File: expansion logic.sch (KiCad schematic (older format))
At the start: 30 parts, among them U302 74LS32, U800 BUSTER5721, U801 MSM6242, U802 74LS138, U803 74LS08, U804 74LS148, Y800 32768Hz

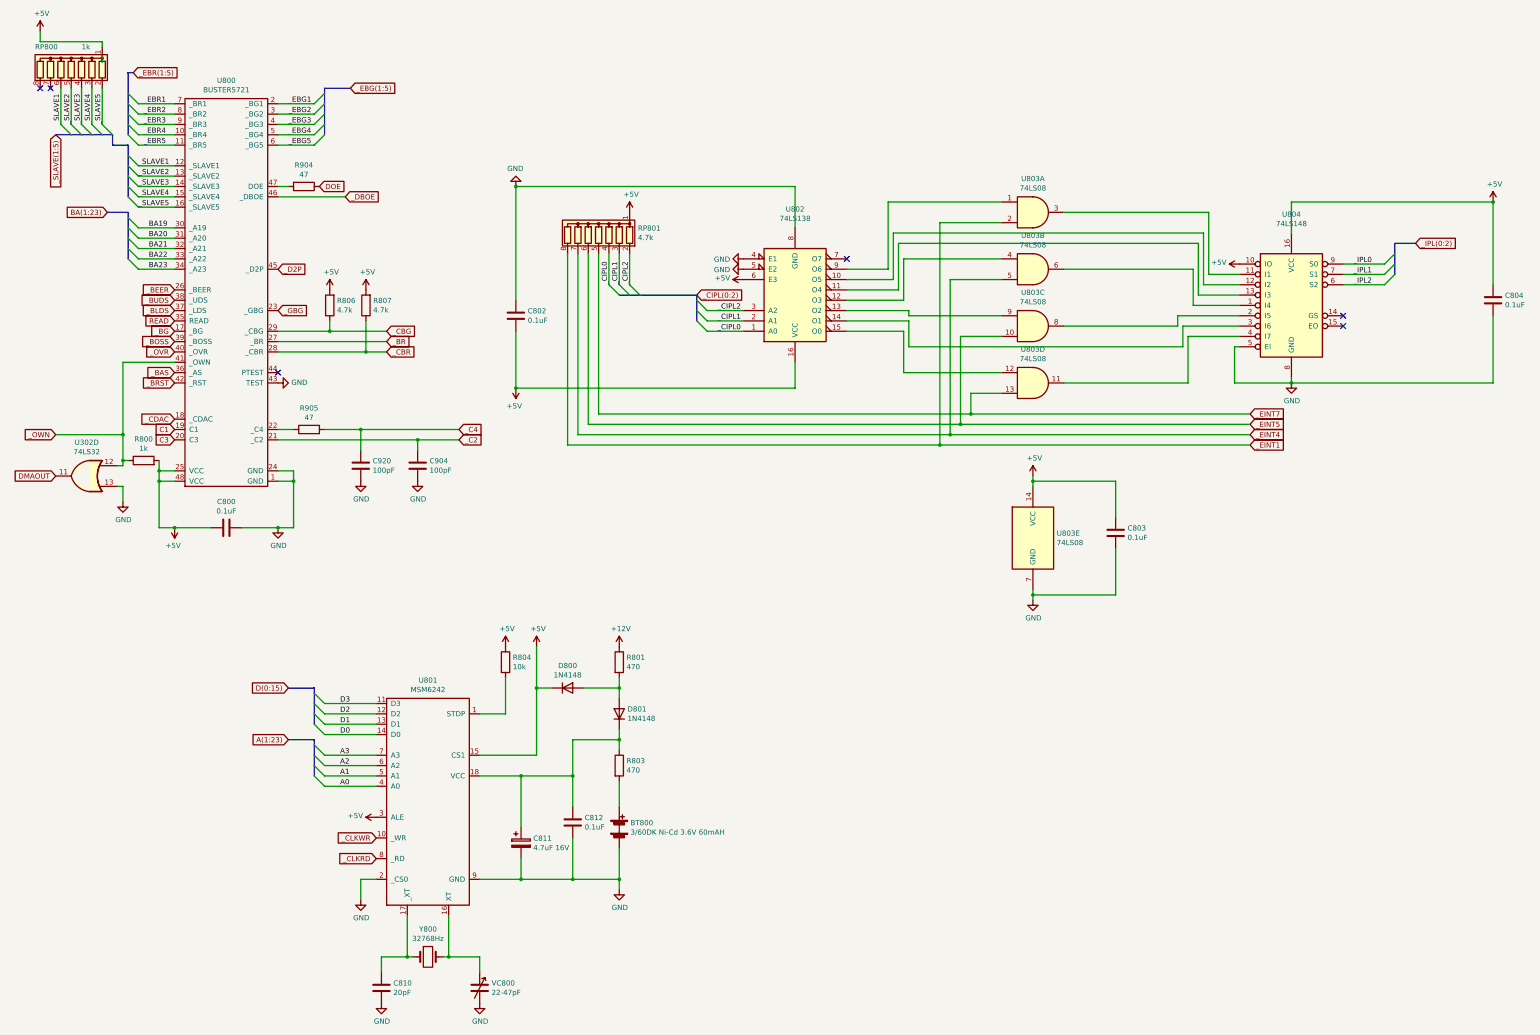
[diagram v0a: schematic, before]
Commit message: Rename bus with correct syntax
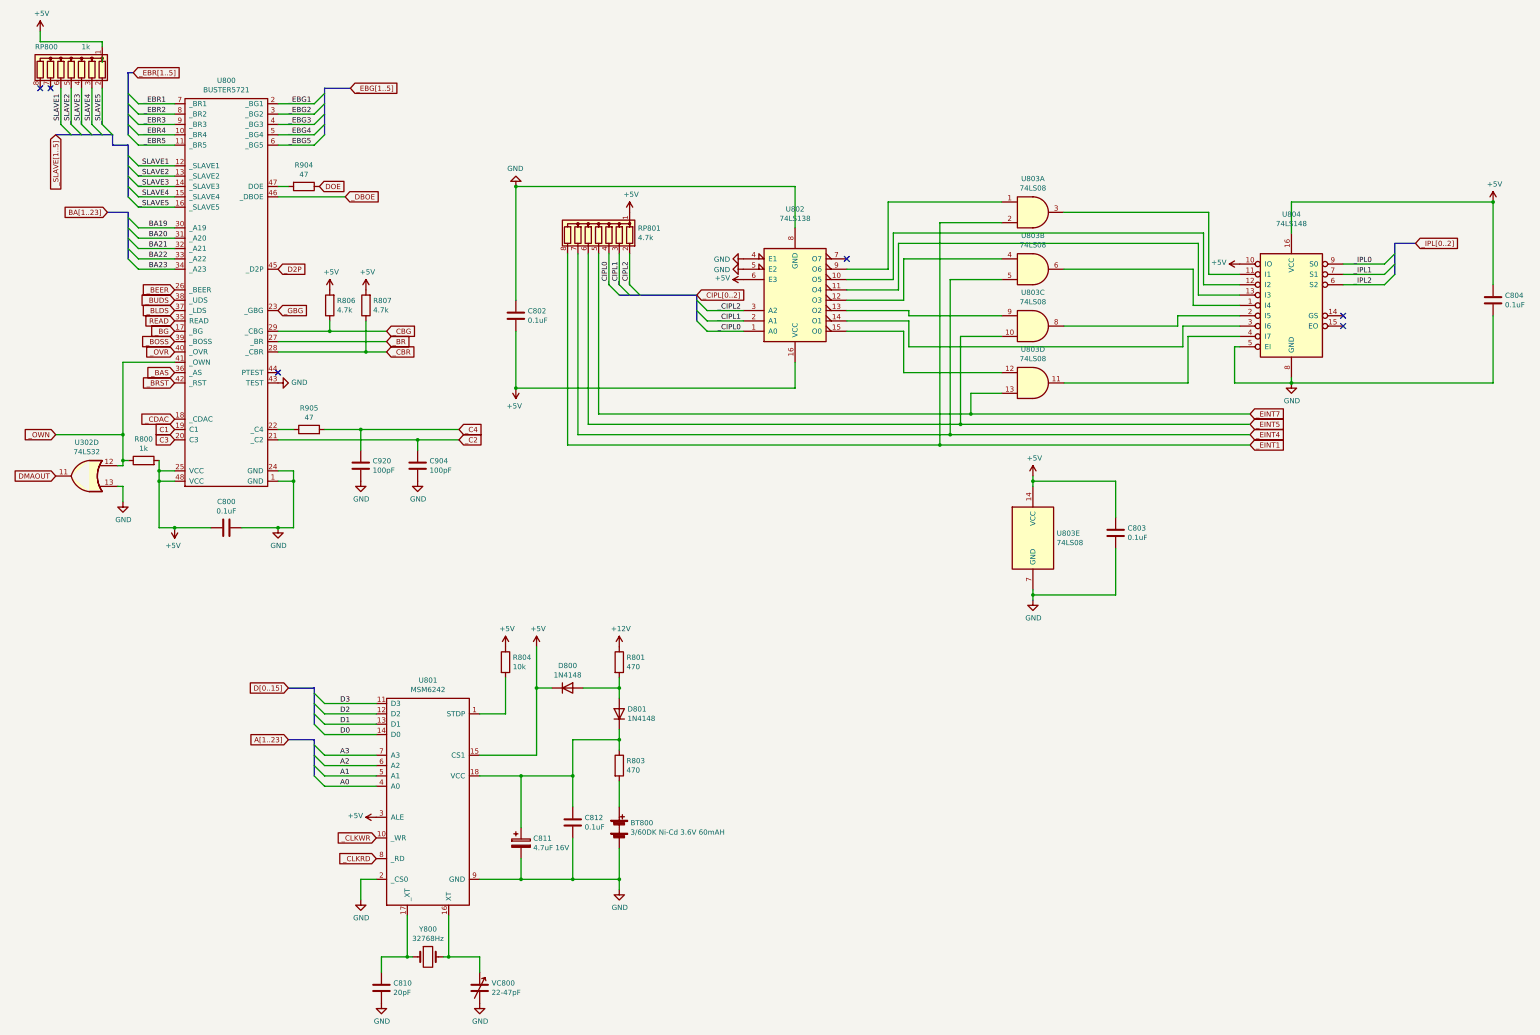
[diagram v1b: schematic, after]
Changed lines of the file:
@@
-EESchema Schematic File Version 4
+EESchema Schematic File Version 5
 LIBS:amiga2000-cache
 EELAYER 29 0
@@
 	1550 1700 1650 1800
 Text GLabel 1600 1100 2    50   Input ~ 0
-_EBR(1:5)
+_EBR[1..5]
 Wire Wire Line
 	3000 1400 3350 1400
@@
 	3350 1800 3450 1700
 Text GLabel 3700 1250 2    50   Input ~ 0
-_EBG(1:5)
+_EBG[1..5]
 Wire Bus Line
 	3700 1250 3450 1250
@@
 	1550 2900 1650 3000
 Text GLabel 1350 2450 0    50   Input ~ 0
-BA(1:23)
+BA[1..23]
 Wire Bus Line
 	1350 2450 1550 2450
@@
 	1400 1800 1400 1700
 Text GLabel 850  1700 3    50   Input ~ 0
-_SLAVE(1:5)
+_SLAVE[1..5]
 NoConn ~ 700  1250
 NoConn ~ 800  1250
@@
 	3350 7900 3450 8000
 Text GLabel 3100 7050 0    50   Input ~ 0
-D(0:15)
+D[0..15]
 Text GLabel 3100 7550 0    50   Input ~ 0
-A(1:23)
+A[1..23]
 Wire Bus Line
 	3100 7050 3350 7050
@@
 	6400 3150 6500 3250
 Text GLabel 7050 3250 2    50   Input ~ 0
-_CIPL(0:2)
+_CIPL[0..2]
 Text Label 13400 2950 0    50   ~ 0
 _IPL0
@@
 	13700 3150 13800 3050
 Text GLabel 14000 2750 2    50   Input ~ 0
-_IPL(0:2)
+_IPL[0..2]
 Wire Bus Line
 	14000 2750 13800 2750

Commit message: Rename some bus things
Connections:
- net _EBG1 renamed _BG1
- net _EBG2 renamed _BG2
- net _EBG3 renamed _BG3
- net _EBG4 renamed _BG4
- net _EBG5 renamed _BG5
- net _EBR1 renamed _BR1
- net _EBR2 renamed _BR2
- net _EBR3 renamed _BR3
- net _EBR4 renamed _BR4
- net _EBR5 renamed _BR5
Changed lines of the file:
@@
 	1650 1800 2000 1800
 Text Label 1700 1400 0    50   ~ 0
-_EBR1
+_BR1
 Text Label 1700 1500 0    50   ~ 0
-_EBR2
+_BR2
 Text Label 1700 1600 0    50   ~ 0
-_EBR3
+_BR3
 Text Label 1700 1700 0    50   ~ 0
-_EBR4
+_BR4
 Text Label 1700 1800 0    50   ~ 0
-_EBR5
+_BR5
 Entry Wire Line
 	1550 1300 1650 1400
@@
 	1550 1700 1650 1800
 Text GLabel 1600 1100 2    50   Input ~ 0
-_EBR[1..5]
+_BR[1..5]
 Wire Wire Line
 	3000 1400 3350 1400
@@
 	3000 1800 3350 1800
 Text Label 3100 1400 0    50   ~ 0
-_EBG1
+_BG1
 Text Label 3100 1500 0    50   ~ 0
-_EBG2
+_BG2
 Text Label 3100 1600 0    50   ~ 0
-_EBG3
+_BG3
 Text Label 3100 1700 0    50   ~ 0
-_EBG4
+_BG4
 Text Label 3100 1800 0    50   ~ 0
-_EBG5
+_BG5
 Entry Wire Line
 	3350 1400 3450 1300
@@
 	3350 1800 3450 1700
 Text GLabel 3700 1250 2    50   Input ~ 0
-_EBG[1..5]
+_BG[1..5]
 Wire Bus Line
 	3700 1250 3450 1250

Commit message: Fix a bunch of DRC errors
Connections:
- net A0 is gone; now on net A2: U801.4 (A0)
- net A1 is gone; now on net A3: U801.5 (A1)
- net A2: no longer U801.6 (A2)
- net A3: no longer U801.7 (A3)
- new net A4: U801.6 (A2)
- new net A5: U801.7 (A3)
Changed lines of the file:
@@
 D0
 Text Label 3600 7700 0    50   ~ 0
+A5
+Text Label 3600 7800 0    50   ~ 0
+A4
+Text Label 3600 7900 0    50   ~ 0
 A3
-Text Label 3600 7800 0    50   ~ 0
+Text Label 3600 8000 0    50   ~ 0
 A2
-Text Label 3600 7900 0    50   ~ 0
-A1
-Text Label 3600 8000 0    50   ~ 0
-A0
 Entry Wire Line
 	3350 7100 3450 7200

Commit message: More final ERC fixes
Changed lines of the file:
@@
 Wire Bus Line
 	3350 7550 3350 7900
+$Comp
+L power:PWR_FLAG #FLG0106
+U 1 1 5DAEC13B
+P 6300 7550
+F 0 "#FLG0106" H 6300 7625 50  0001 C CNN
+F 1 "PWR_FLAG" V 6300 7678 50  0000 L CNN
+F 2 "" H 6300 7550 50  0001 C CNN
+F 3 "~" H 6300 7550 50  0001 C CNN
+	1    6300 7550
+	0    1    1    0
+$EndComp
 $EndSCHEMATC
